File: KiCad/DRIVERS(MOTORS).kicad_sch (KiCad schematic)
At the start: 15 parts, among them M1 Motor_DC, M2 Motor_DC, M3 Motor_DC, U1 TB6612FNG, U2 TB6612FNG, U3 TB6612FNG

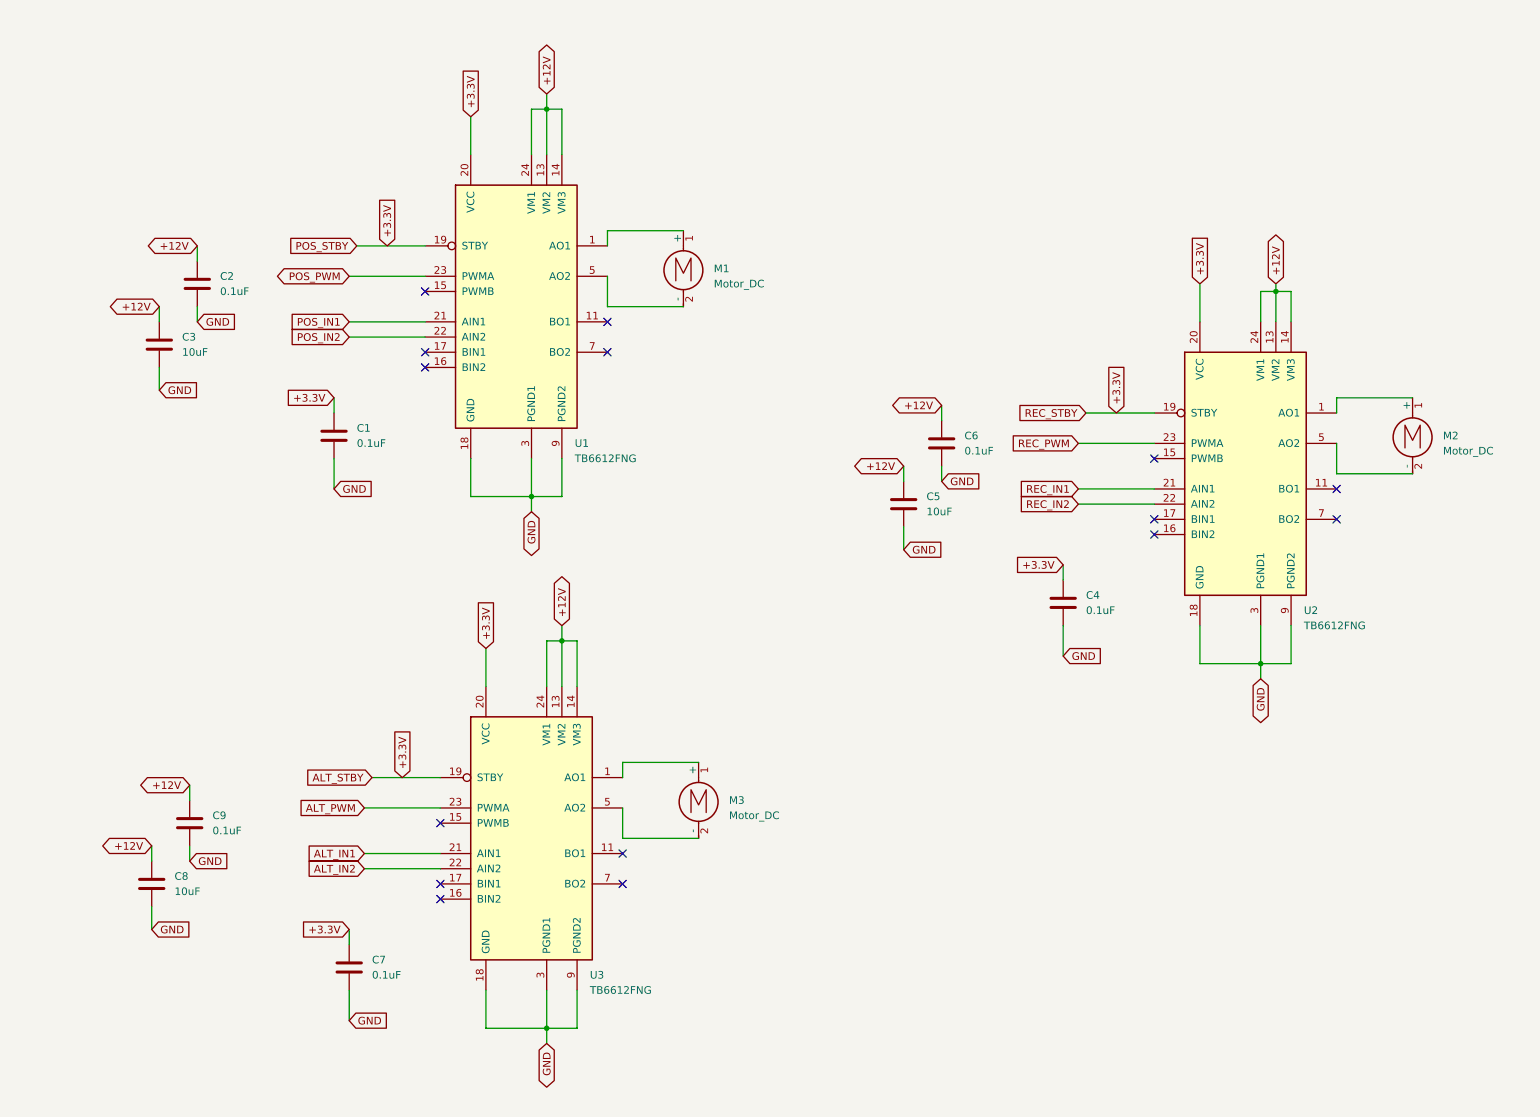
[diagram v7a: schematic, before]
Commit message: Afegist el MOSFET
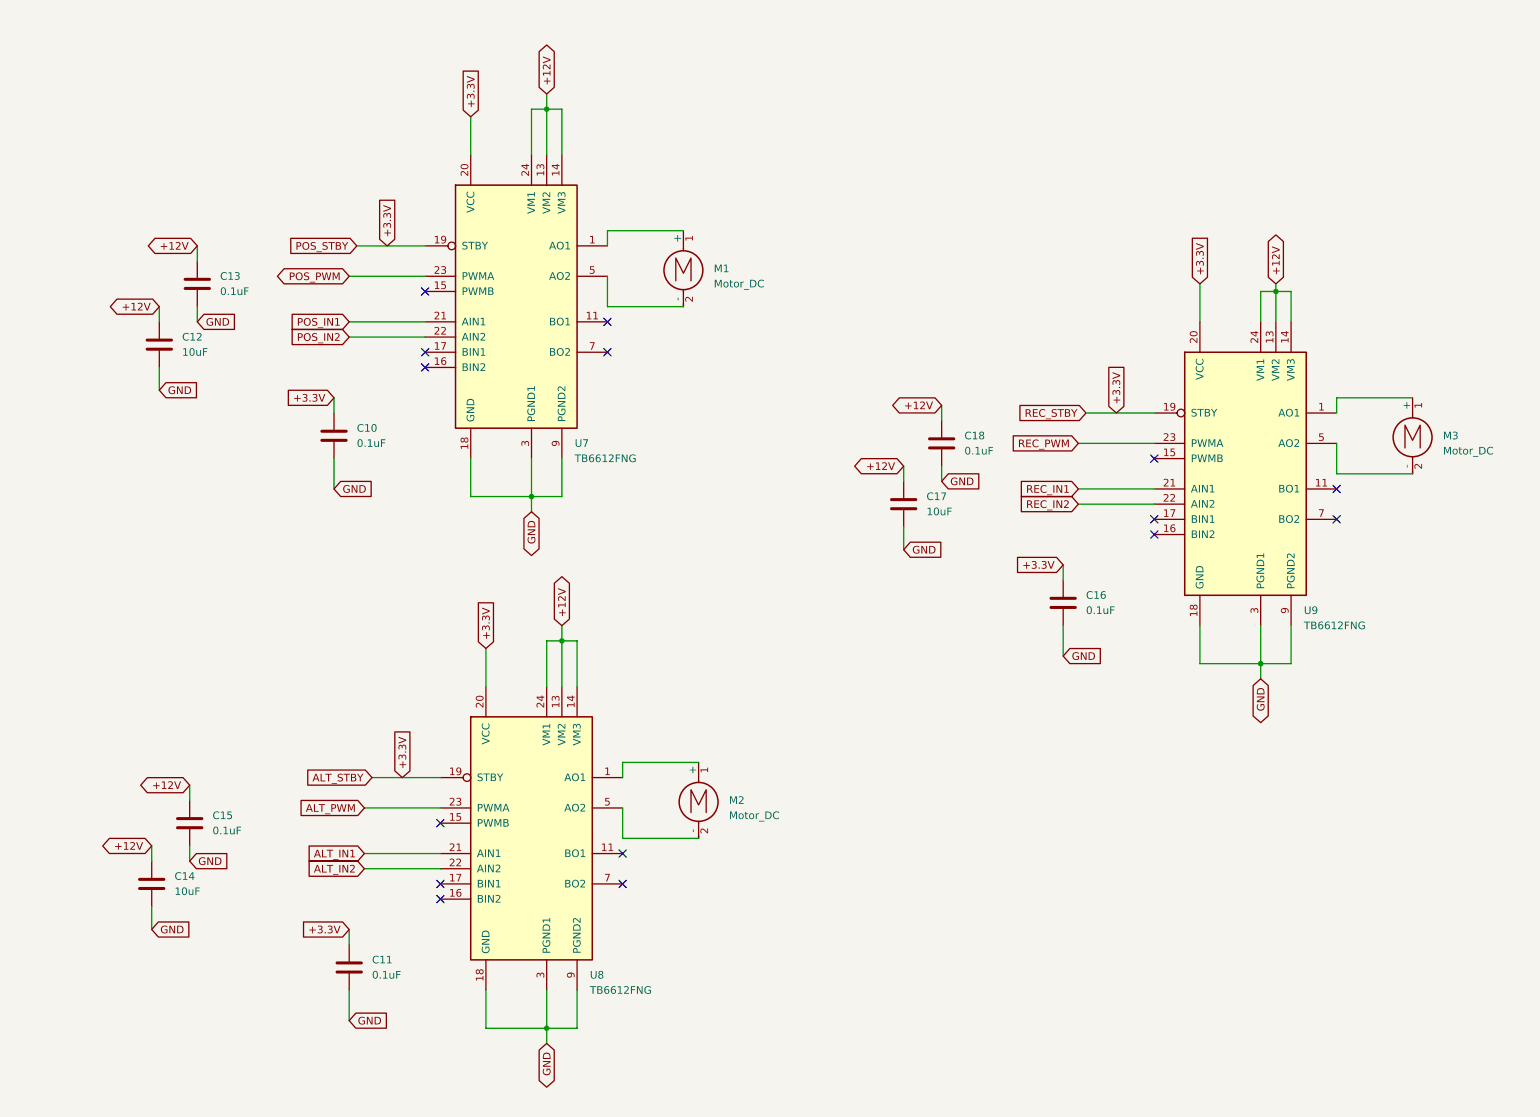
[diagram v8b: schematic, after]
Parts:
- renumbered C1 to C10, C7 to C11, C3 to C12, C2 to C13, C8 to C14, C9 to C15, C4 to C16, C5 to C17, C6 to C18, M3 to M2, M2 to M3, U1 to U7, U3 to U8, U2 to U9
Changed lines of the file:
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@@
 		(dnp no)
 		(fields_autoplaced yes)
-		(property "Reference" "C5"
+		(property "Reference" "C17"
 			(at 184.15 92.7099 0)
 			(effects
@@
 		(dnp no)
 		(fields_autoplaced yes)
-		(property "Reference" "M2"
+		(property "Reference" "M3"
 			(at 270.51 82.5499 0)
 			(effects
@@
 		(dnp no)
 		(fields_autoplaced yes)
-		(property "Reference" "C3"
+		(property "Reference" "C12"
 			(at 59.69 66.0399 0)
 			(effects
@@
 		(dnp no)
 		(fields_autoplaced yes)
-		(property "Reference" "C6"
+		(property "Reference" "C18"
 			(at 190.5 82.5499 0)
 			(effects
@@
 		(dnp no)
 		(fields_autoplaced yes)
-		(property "Reference" "M3"
+		(property "Reference" "M2"
 			(at 151.13 143.5099 0)
 			(effects
@@
 		(dnp no)
 		(fields_autoplaced yes)
-		(property "Reference" "C7"
+		(property "Reference" "C11"
 			(at 91.44 170.1799 0)
 			(effects
@@
 		(dnp no)
 		(fields_autoplaced yes)
-		(property "Reference" "C4"
+		(property "Reference" "C16"
 			(at 210.82 109.2199 0)
 			(effects
@@
 		(dnp no)
 		(fields_autoplaced yes)
-		(property "Reference" "U2"
+		(property "Reference" "U9"
 			(at 247.2533 111.76 0)
 			(effects
@@
 		(dnp no)
 		(fields_autoplaced yes)
-		(property "Reference" "U1"
+		(property "Reference" "U7"
 			(at 125.3333 83.82 0)
 			(effects
@@
 		(dnp no)
 		(fields_autoplaced yes)
-		(property "Reference" "C8"
+		(property "Reference" "C14"
 			(at 58.42 156.2099 0)
 			(effects
@@
 		(dnp no)
 		(fields_autoplaced yes)
-		(property "Reference" "C2"
+		(property "Reference" "C13"
 			(at 66.04 55.8799 0)
 			(effects
@@
 		(dnp no)
 		(fields_autoplaced yes)
-		(property "Reference" "U3"
+		(property "Reference" "U8"
 			(at 127.8733 172.72 0)
 			(effects
@@
 		(dnp no)
 		(fields_autoplaced yes)
-		(property "Reference" "C9"
+		(property "Reference" "C15"
 			(at 64.77 146.0499 0)
 			(effects
@@
 		(dnp no)
 		(fields_autoplaced yes)
-		(property "Reference" "C1"
+		(property "Reference" "C10"
 			(at 88.9 81.2799 0)
 			(effects
